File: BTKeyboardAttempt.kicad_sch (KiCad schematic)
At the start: 137 parts, among them J1 USB_C_Receptacle, SW1 SW_Push, U2 ATmega32U4-A, Y1 Crystal_GND24_Small

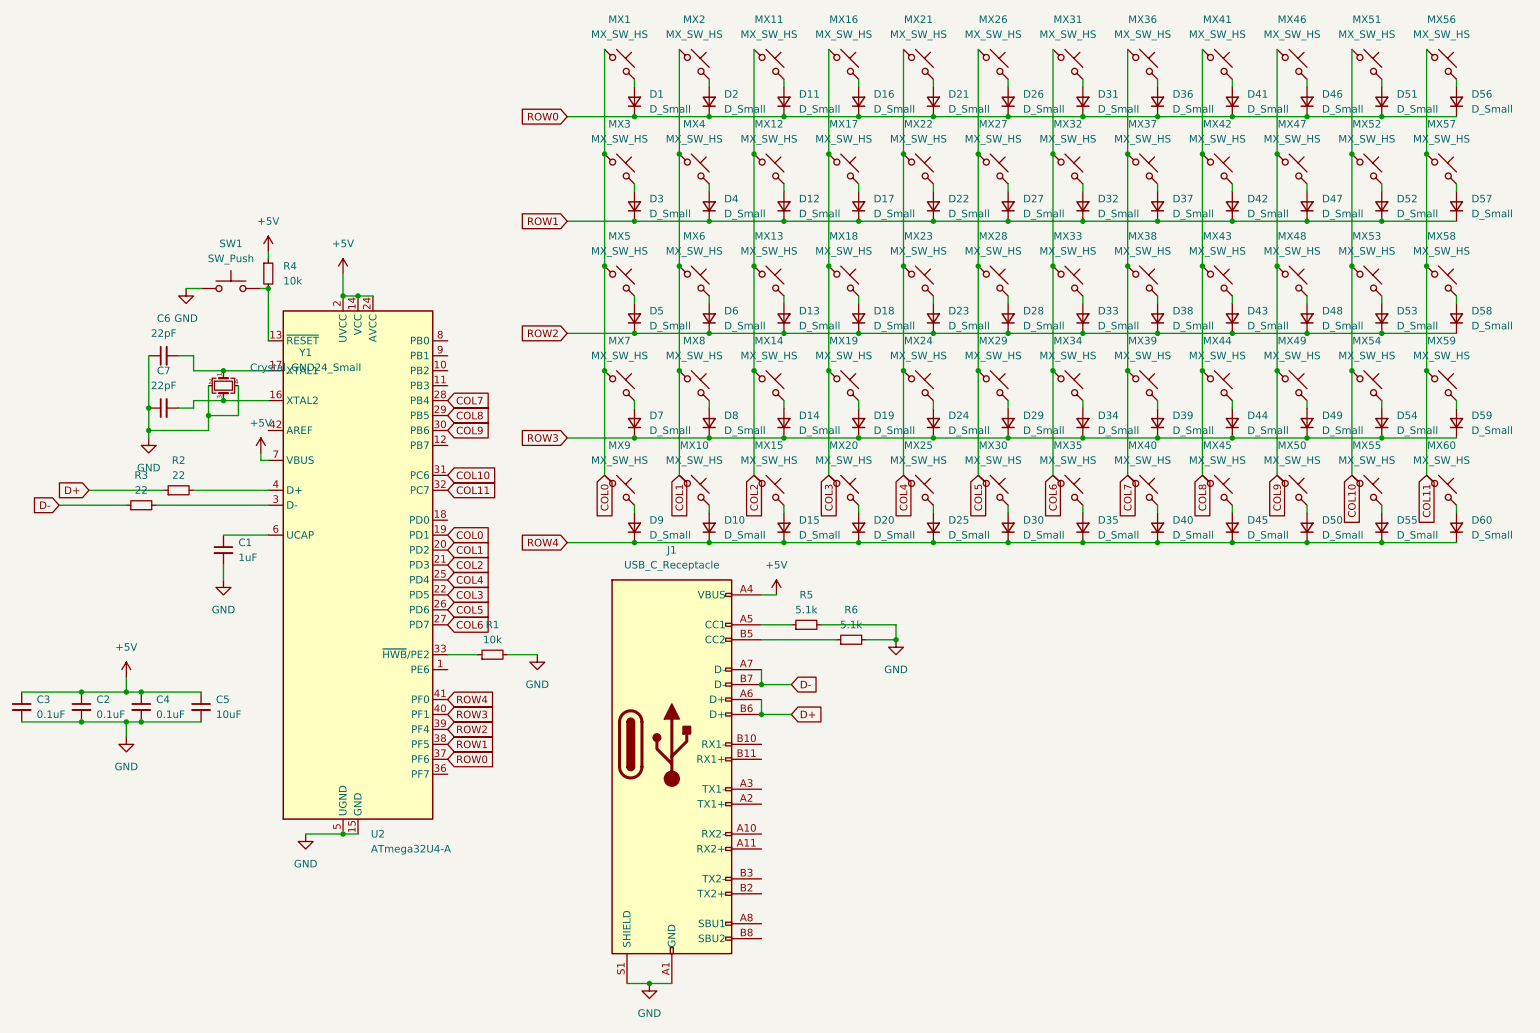
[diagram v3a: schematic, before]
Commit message: Daughter board
Put MCU and USB-C (+assoc. bits) on a daughter board to reduce overall footprint of pcb
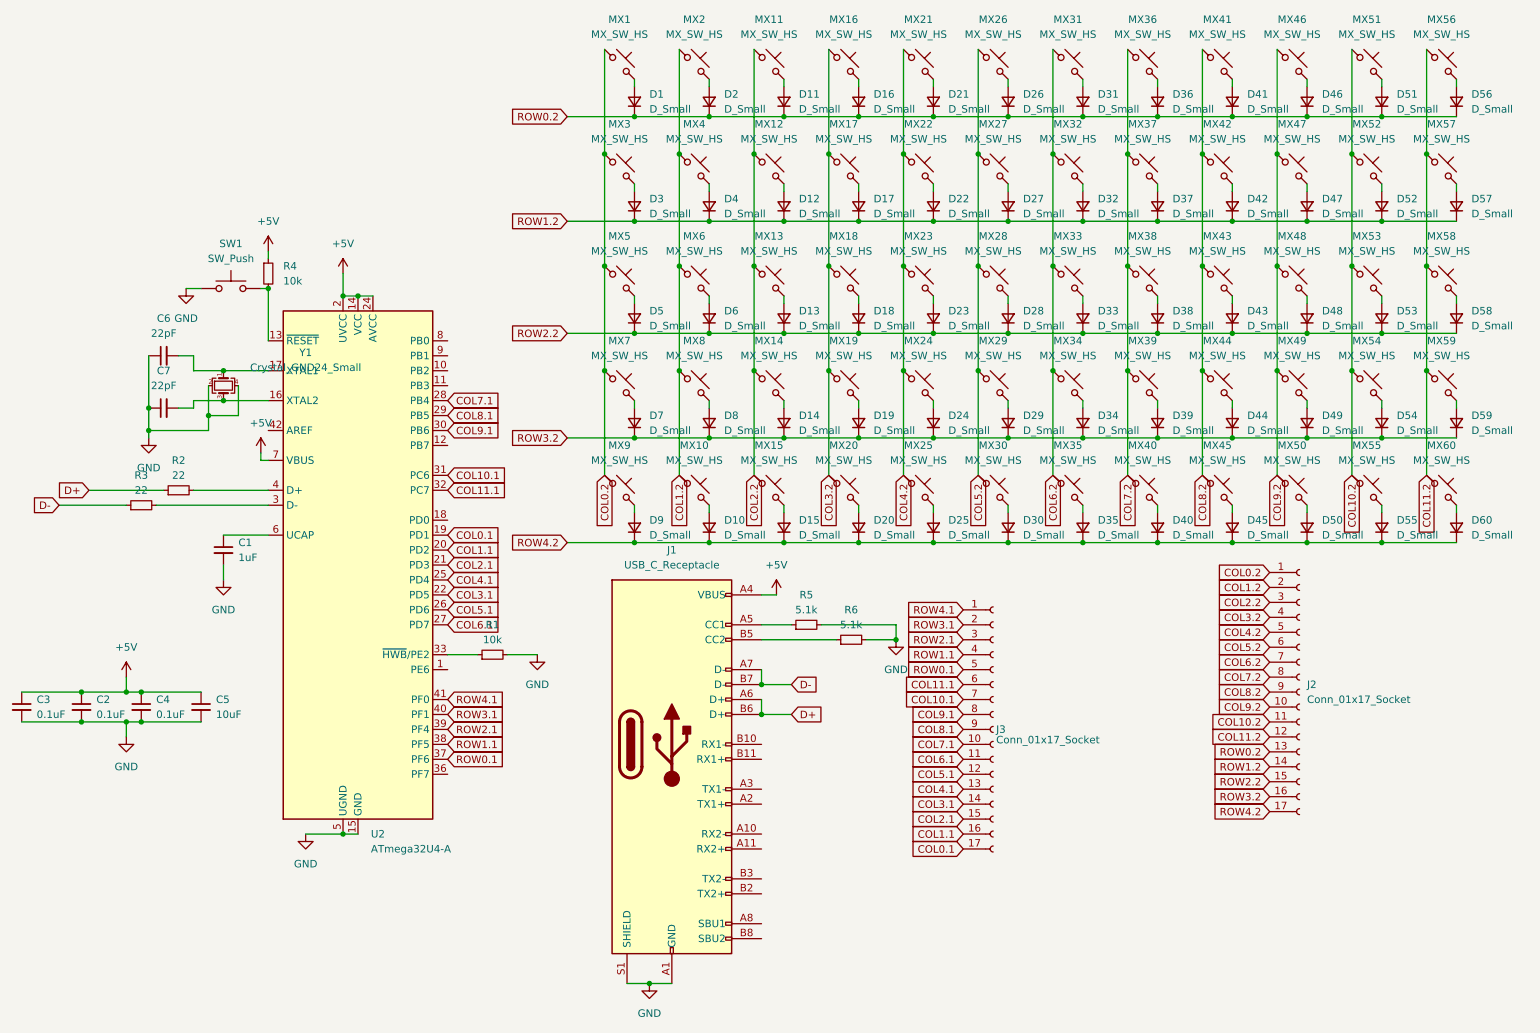
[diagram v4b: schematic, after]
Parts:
- added J2, J3: Conn_01x17_Socket, Connector_PinHeader_1.00mm:PinHeader_1x17_P1.00mm_Horizontal, symbol Connector:Conn_01x17_Socket
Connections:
- net COL0 renamed COL0.2
- net COL0.2: now also J2.1 (Pin_1); no longer U2.19 (PD1)
- net COL1 renamed COL1.2
- net COL1.2: now also J2.2 (Pin_2); no longer U2.20 (PD2)
- net COL10 renamed COL10.2
- net COL10.2: now also J2.11 (Pin_11); no longer U2.31 (PC6)
- net COL11 renamed COL11.2
- net COL11.2: now also J2.12 (Pin_12); no longer U2.32 (PC7)
- net COL2 renamed COL2.2
- net COL2.2: now also J2.3 (Pin_3); no longer U2.21 (PD3)
- net COL3 renamed COL3.2
- net COL3.2: now also J2.4 (Pin_4); no longer U2.22 (PD5)
- net COL4 renamed COL4.2
- net COL4.2: now also J2.5 (Pin_5); no longer U2.25 (PD4)
- net COL5 renamed COL5.2
- net COL5.2: now also J2.6 (Pin_6); no longer U2.26 (PD6)
- net COL6 renamed COL6.2
- net COL6.2: now also J2.7 (Pin_7); no longer U2.27 (PD7)
- net COL7 renamed COL7.2
- net COL7.2: now also J2.8 (Pin_8); no longer U2.28 (PB4)
- net COL8 renamed COL8.2
- net COL8.2: now also J2.9 (Pin_9); no longer U2.29 (PB5)
- net COL9 renamed COL9.2
- net COL9.2: now also J2.10 (Pin_10); no longer U2.30 (PB6)
- net ROW0 renamed ROW0.2
- net ROW0.2: now also J2.13 (Pin_13); no longer U2.37 (PF6)
- net ROW1 renamed ROW1.2
- net ROW1.2: now also J2.14 (Pin_14); no longer U2.38 (PF5)
- net ROW2 renamed ROW2.2
- net ROW2.2: now also J2.15 (Pin_15); no longer U2.39 (PF4)
- net ROW3 renamed ROW3.2
- net ROW3.2: now also J2.16 (Pin_16); no longer U2.40 (PF1)
- net ROW4 renamed ROW4.2
- net ROW4.2: now also J2.17 (Pin_17); no longer U2.41 (PF0)
- new net COL0.1: J3.17 (Pin_17), U2.19 (PD1)
- new net COL1.1: J3.16 (Pin_16), U2.20 (PD2)
- new net COL10.1: J3.7 (Pin_7), U2.31 (PC6)
- new net COL11.1: J3.6 (Pin_6), U2.32 (PC7)
- new net COL2.1: J3.15 (Pin_15), U2.21 (PD3)
- new net COL3.1: J3.14 (Pin_14), U2.22 (PD5)
- new net COL4.1: J3.13 (Pin_13), U2.25 (PD4)
- new net COL5.1: J3.12 (Pin_12), U2.26 (PD6)
- new net COL6.1: J3.11 (Pin_11), U2.27 (PD7)
- new net COL7.1: J3.10 (Pin_10), U2.28 (PB4)
- new net COL8.1: J3.9 (Pin_9), U2.29 (PB5)
- new net COL9.1: J3.8 (Pin_8), U2.30 (PB6)
- new net ROW0.1: J3.5 (Pin_5), U2.37 (PF6)
- new net ROW1.1: J3.4 (Pin_4), U2.38 (PF5)
- new net ROW2.1: J3.3 (Pin_3), U2.39 (PF4)
- new net ROW3.1: J3.2 (Pin_2), U2.40 (PF1)
- new net ROW4.1: J3.1 (Pin_1), U2.41 (PF0)
